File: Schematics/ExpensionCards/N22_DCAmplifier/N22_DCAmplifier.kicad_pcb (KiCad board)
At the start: 2 copper layers, 100.5 x 66.5 mm, 81 parts

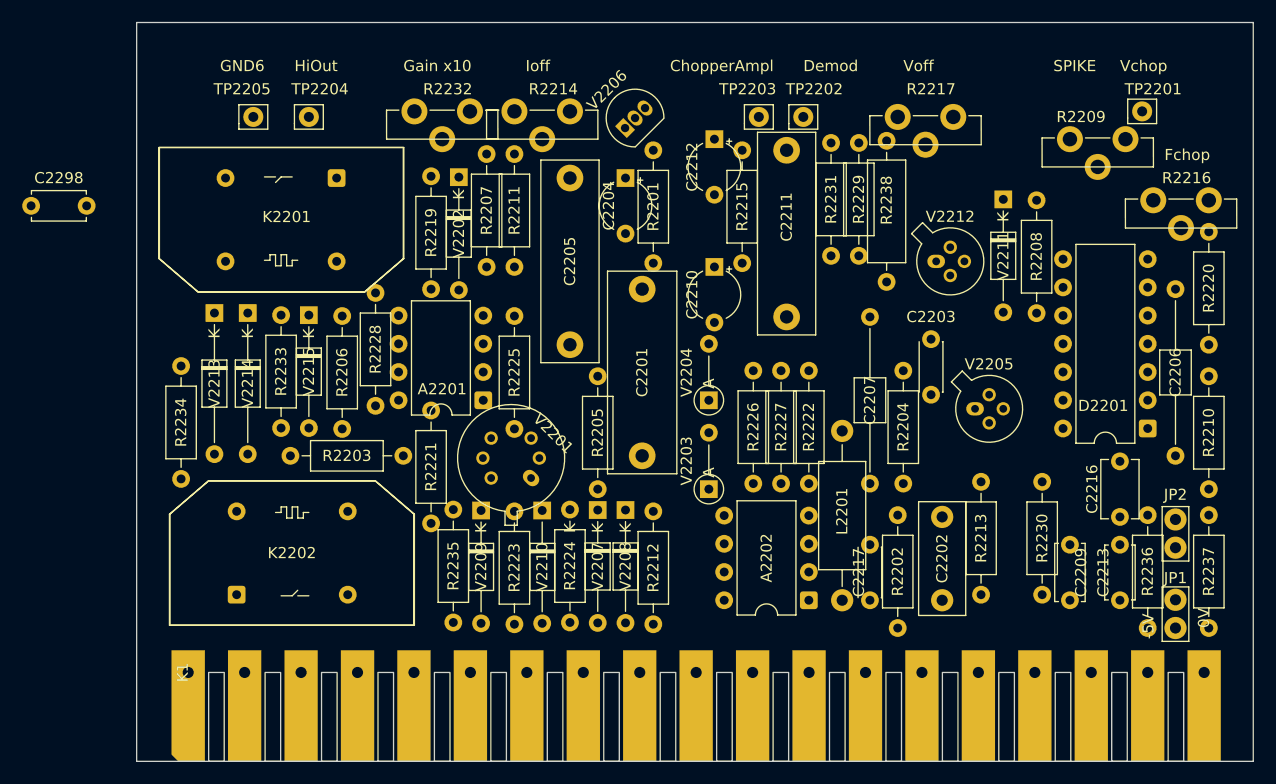
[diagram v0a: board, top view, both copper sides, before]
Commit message: Reworked N20/N21
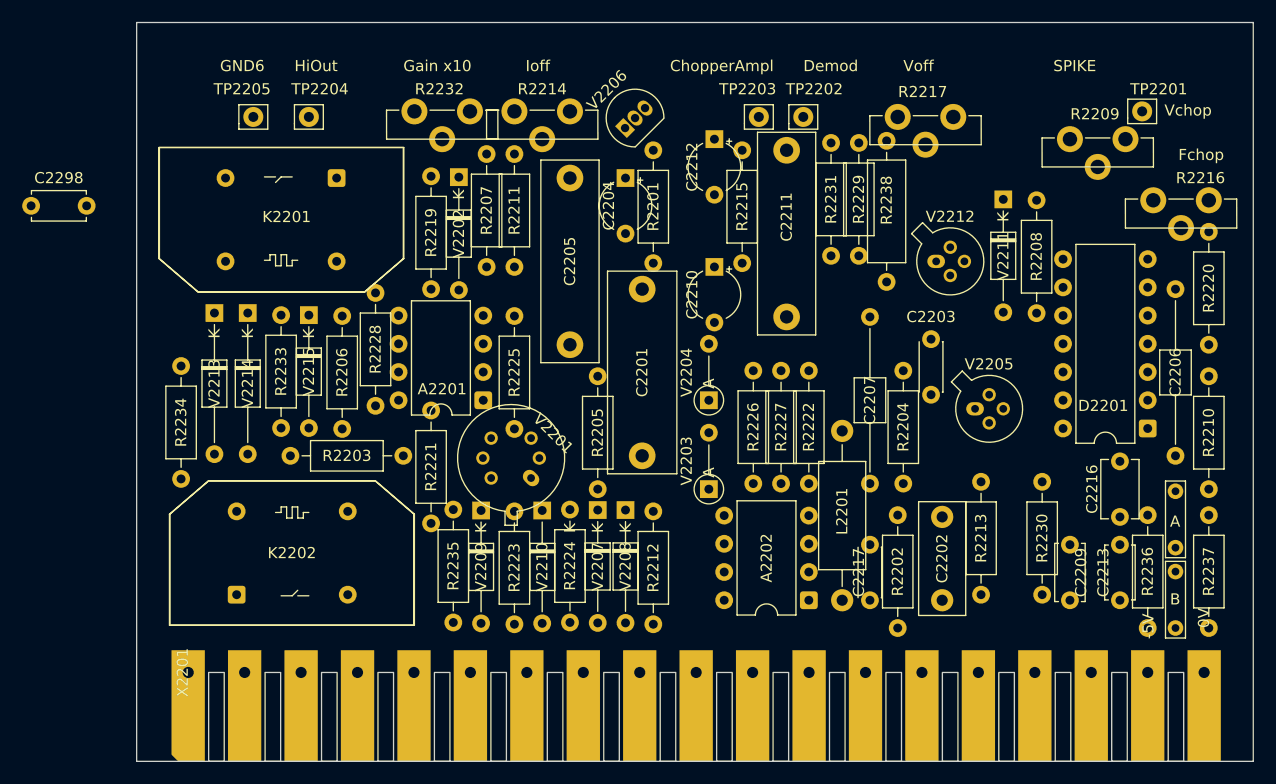
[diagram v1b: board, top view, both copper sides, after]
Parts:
- JP2201: renamed from JP2; footprint TestPoint:TestPoint_Bridge_Pitch2.54mm_Drill1.0mm -> TestPoint:TestPoint_Bridge_Pitch5.08mm_Drill0.7mm
- JP2202: renamed from JP1; footprint TestPoint:TestPoint_Bridge_Pitch2.54mm_Drill1.0mm -> TestPoint:TestPoint_Bridge_Pitch5.08mm_Drill0.7mm
- R2209, R2214, R2216, R2217, R2232: footprint PM2528:Potentiometer horizontal ceramic -> PM2528:Trimmer vertical
- renumbered K1 to X2201
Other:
- board text added: "A"
- board text added: "B"

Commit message: Small modifications, more disassembly
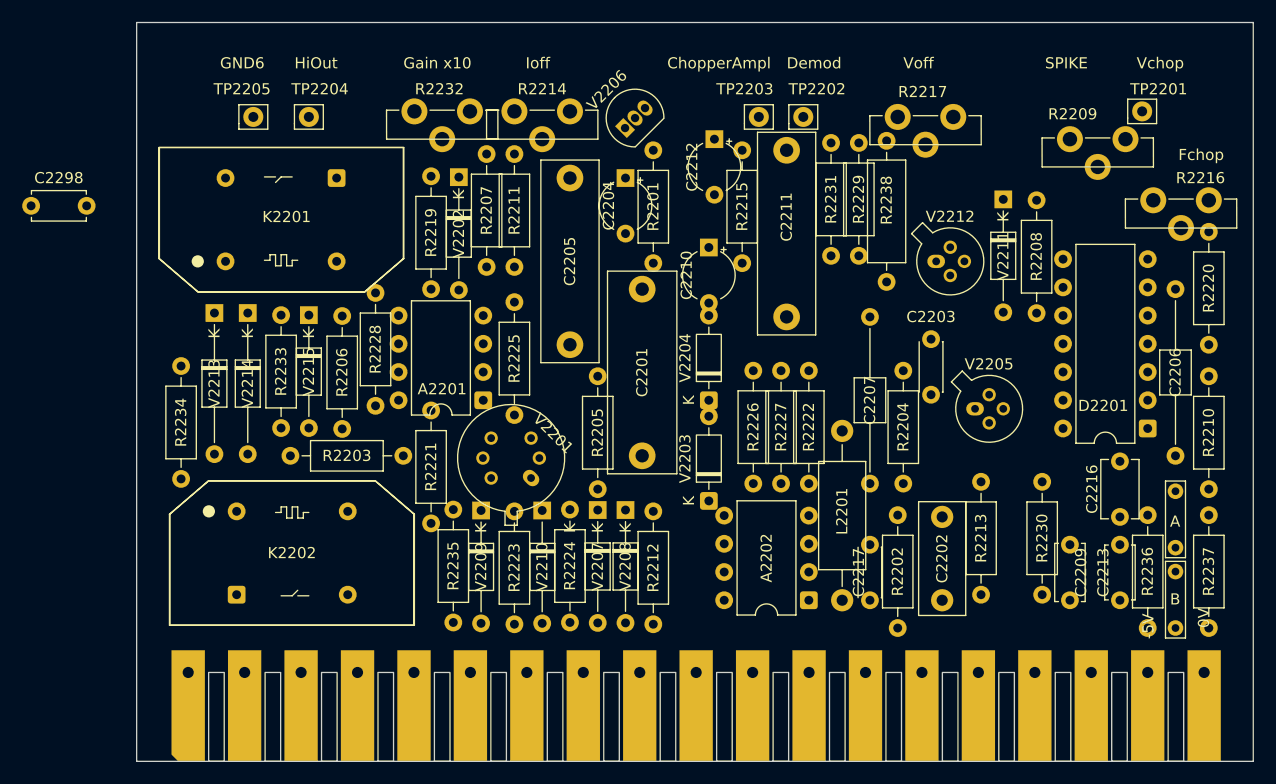
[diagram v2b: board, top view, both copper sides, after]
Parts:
- V2203, V2204: footprint Diode_THT:D_DO-35_SOD27_P5.08mm_Vertical_AnodeUp -> Diode_THT:D_DO-35_SOD27_P7.62mm_Horizontal
- moved C2210 1.82 mm to (153.0, 82.8)
- moved R2225 1.25 mm to (135.5, 97.8)
- moved V2203 1.06 mm to (153.0, 105.6)
